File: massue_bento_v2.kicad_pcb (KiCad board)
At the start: 2 copper layers, 100 x 21 mm, 69 parts, among them K1 CONN_3, K2 CONN_3, K3 CONN_3, P1 TST, P10 CONN_1, P11 TST, P12 TST, P13 TST, P14 TST, P15 TST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

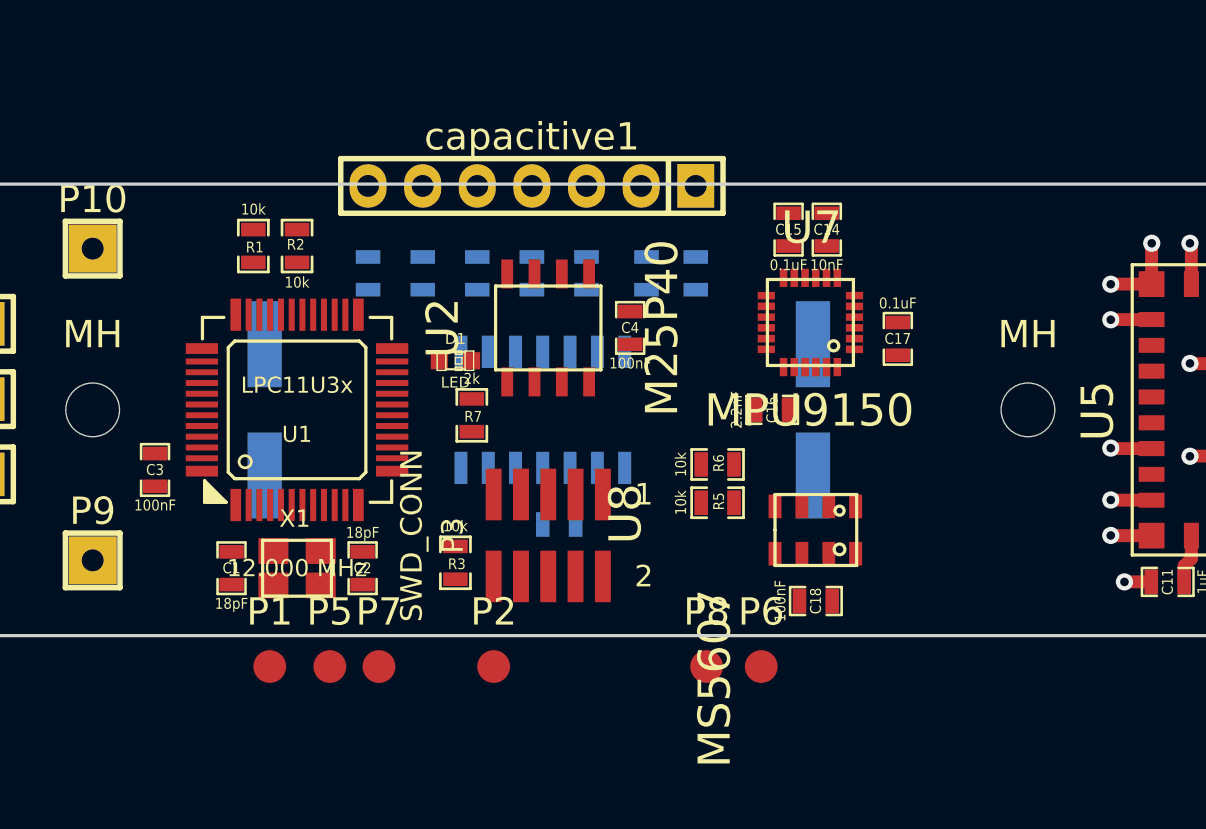
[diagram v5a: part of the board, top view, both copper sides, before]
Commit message: New component placement
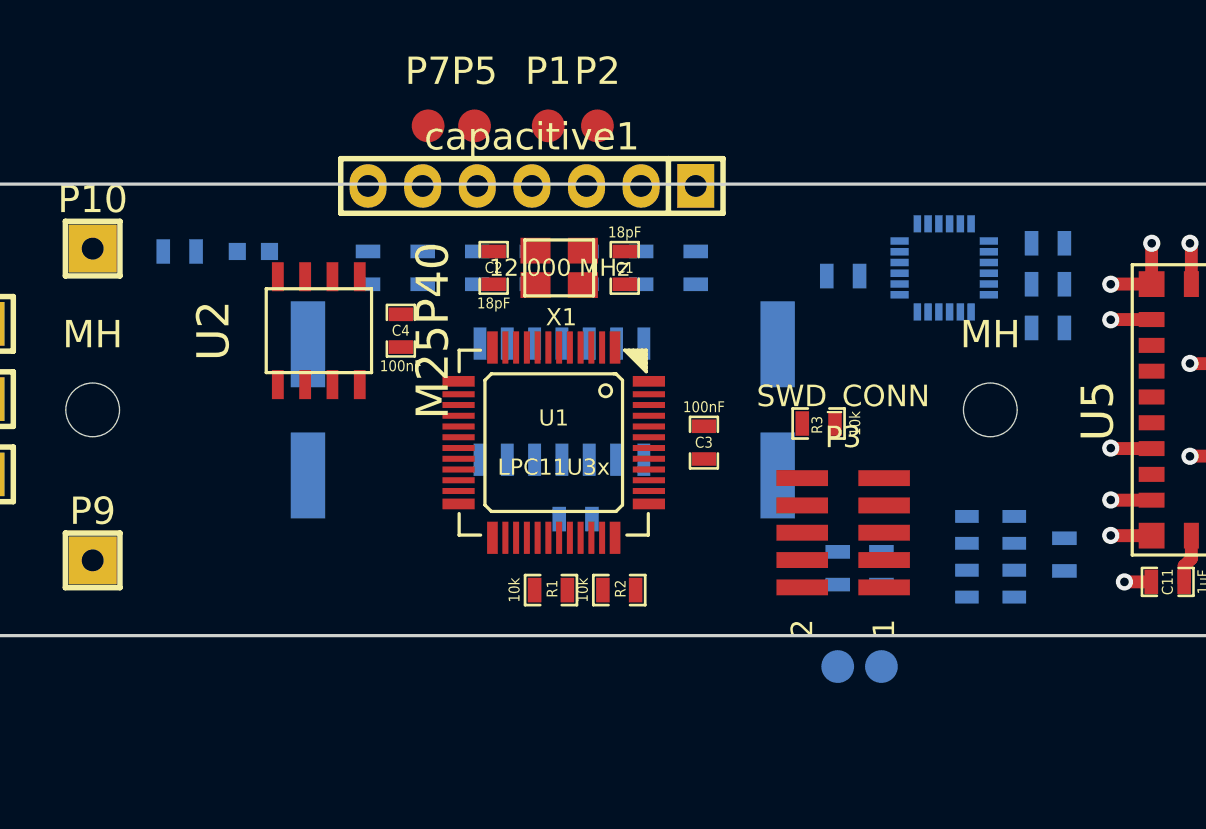
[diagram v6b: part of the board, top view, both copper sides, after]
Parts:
- C14, C15, C16, C17, C18, D1, P6, P8, R5, R6, R7, U7, U8: moved to B.Cu
- moved P1 28.3 mm to (145.2, 96.8)
- moved P5 26.0 mm to (141.8, 96.8)
- moved P2 25.6 mm to (147.5, 96.8)
- moved C3 25.6 mm to (152.4, 111.5), turned to 270 degrees
- moved P7 25.2 mm to (139.6, 96.8)
- moved C1 23.0 mm to (148.7, 103.4), turned to 270 degrees
- moved R2 21.9 mm to (148.5, 118.4), turned to 0 degrees
- moved R1 21.2 mm to (145.3, 118.4), turned to 0 degrees
- moved X1 18.5 mm to (145.7, 103.4), turned to 180 degrees
- moved R3 18.1 mm to (157.8, 110.6), turned to 180 degrees
- moved R7 15.6 mm to (128.0, 102.6), turned to 180 degrees
- moved C2 15.2 mm to (142.7, 103.4), turned to 90 degrees
- moved P3 13.7 mm to (158.9, 115.7), turned to 180 degrees
- moved C15 12.3 mm to (168.4, 104.2), turned to 0 degrees
- moved U1 12.0 mm to (145.4, 111.5), turned to 180 degrees
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
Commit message: New : Power routing
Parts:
- moved P9 20.5 mm to (109.6, 102.4)
- moved P10 18.2 mm to (105.8, 102.4)
- moved R8 4.50 mm to (103.3, 117.6), turned to 270 degrees
- moved C7 4.13 mm to (103.3, 103.7), turned to 90 degrees
- moved R7 3.52 mm to (131.2, 101.1), turned to 0 degrees
- moved K1 2.41 mm to (116.0, 103.7), turned to 180 degrees
- moved K3 2.14 mm to (116.0, 115.1), turned to 180 degrees
- moved K2 1.84 mm to (116.0, 111.3), turned to 180 degrees
- moved R4 1.37 mm to (104.5, 110.0), turned to 270 degrees
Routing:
- net VBAT: track 2.29 -> 22.6 mm, vias 0 -> 2
- net +3.3V: track 2.17 -> 20.8 mm
- net +5V_USB: track 0.00 -> 15.3 mm
- net GND: track 98.4 -> 111.5 mm, vias 56 -> 3
- net Net-(R12-Pad2): track 0.00 -> 5.63 mm
- net Net-(C2-Pad1): track 0.00 -> 5.11 mm
- net Net-(R17-Pad2): track 0.00 -> 4.61 mm
- net Net-(R13-Pad2): track 0.00 -> 4.36 mm
- net Net-(R16-Pad2): track 0.00 -> 3.34 mm
- net Net-(C7-Pad1): track 0.00 -> 3.08 mm
- net Net-(R18-Pad1): track 0.00 -> 3.05 mm
- net Net-(R17-Pad1): track 0.00 -> 3.05 mm
- net Net-(R16-Pad1): track 0.00 -> 3.05 mm
- net Net-(R15-Pad1): track 0.00 -> 3.05 mm
- net Net-(R14-Pad1): track 0.00 -> 3.05 mm
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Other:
- net class POWER added: clearance 0.3, trace_width 0.7, via_dia 0.8, via_drill 0.4

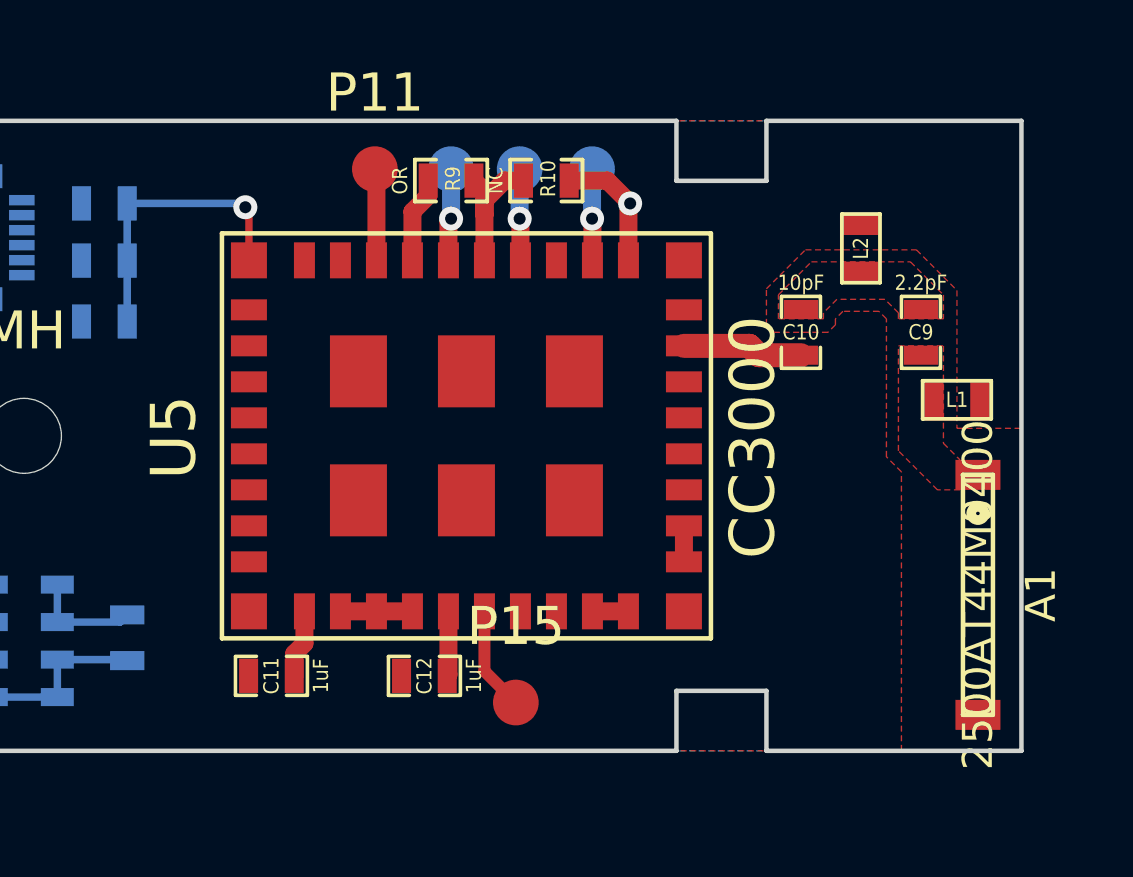
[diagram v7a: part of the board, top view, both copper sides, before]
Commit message: Restore ground routing for CC3000
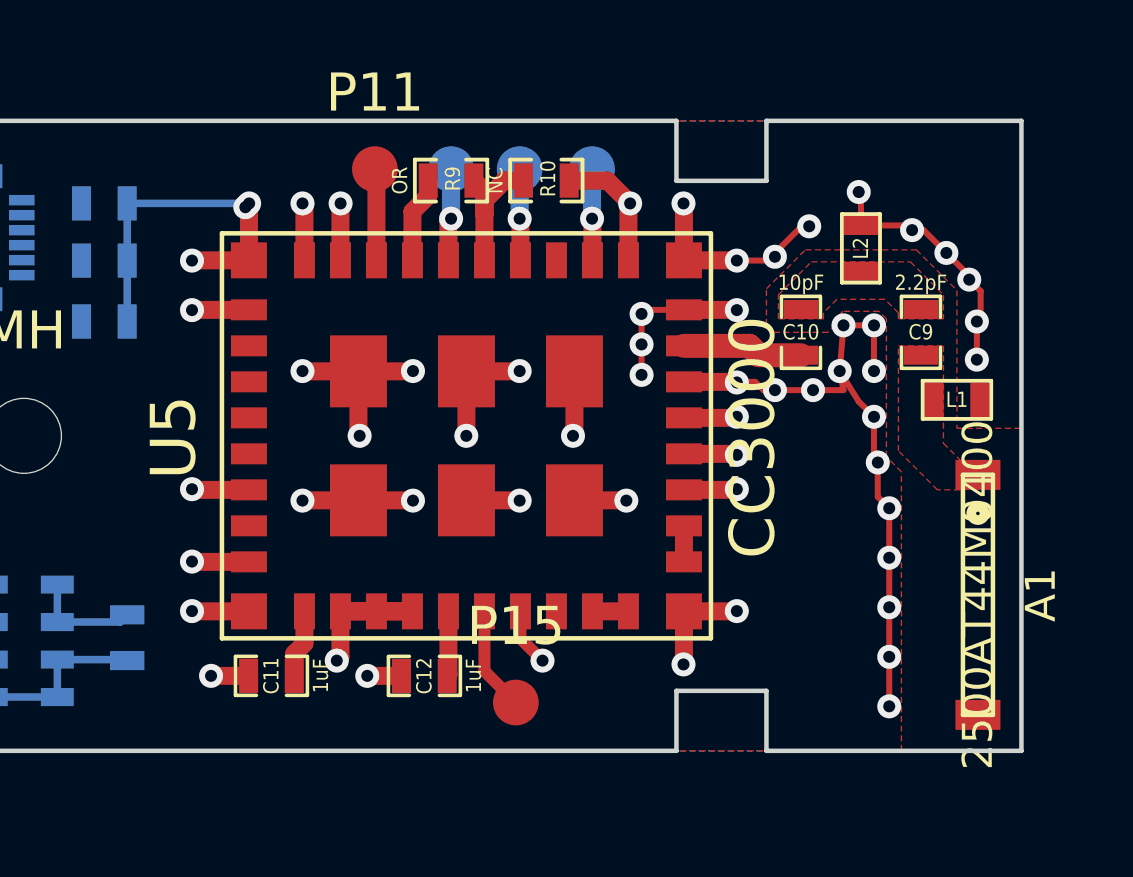
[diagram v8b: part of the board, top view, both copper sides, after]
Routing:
- net GND: track 111.5 -> 205.6 mm, vias 3 -> 58
